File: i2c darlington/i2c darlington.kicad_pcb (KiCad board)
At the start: 2 copper layers, 131.2 x 55 mm, 48 parts, among them IC1 ULN2074B, IC2 ULN2074B, IC3 ULN2074B, IC4 ULN2074B, J1 to qwiic breakout, J2 high current ground, J3 Conn_01x04, J4 Conn_01x04, J5 Conn_01x04, J6 Conn_01x04, J7 Conn_01x01, J8 Conn_01x01, J9 Conn_01x01, U1 PCA9685PW

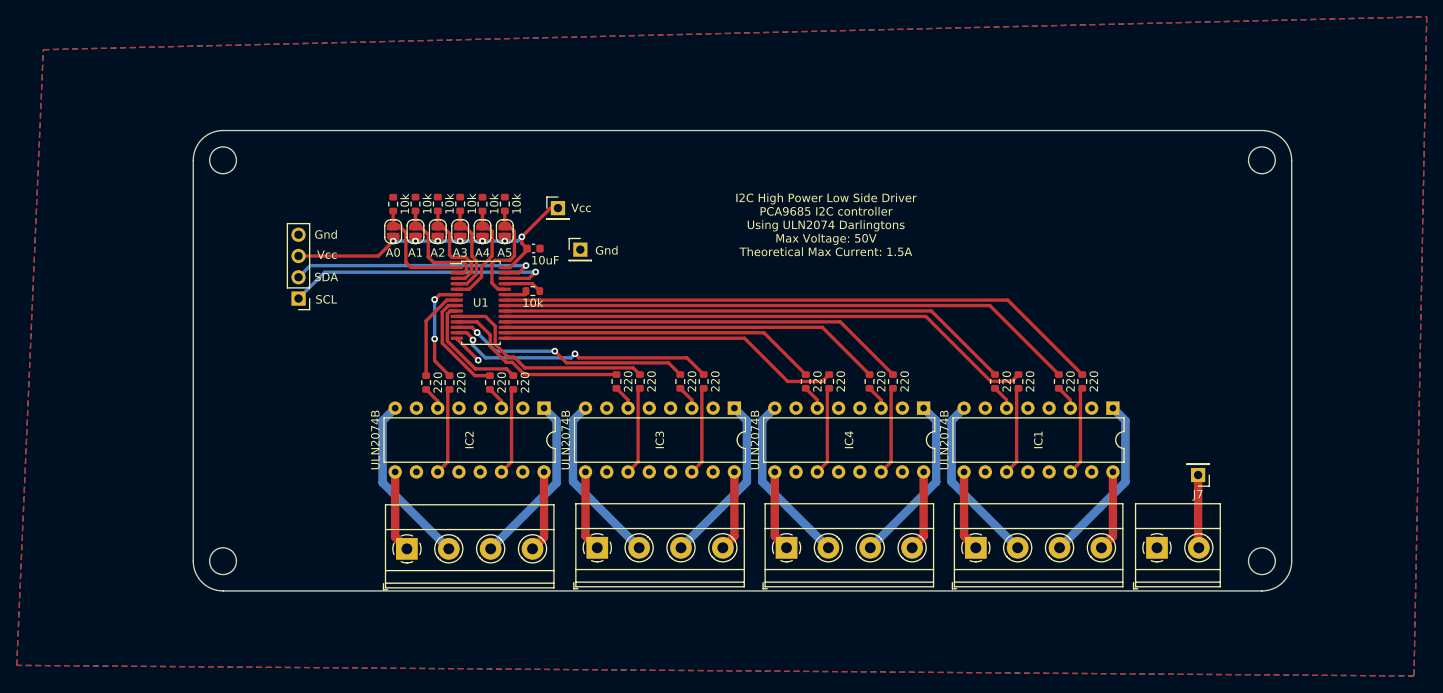
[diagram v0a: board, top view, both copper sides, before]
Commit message: shrank boards
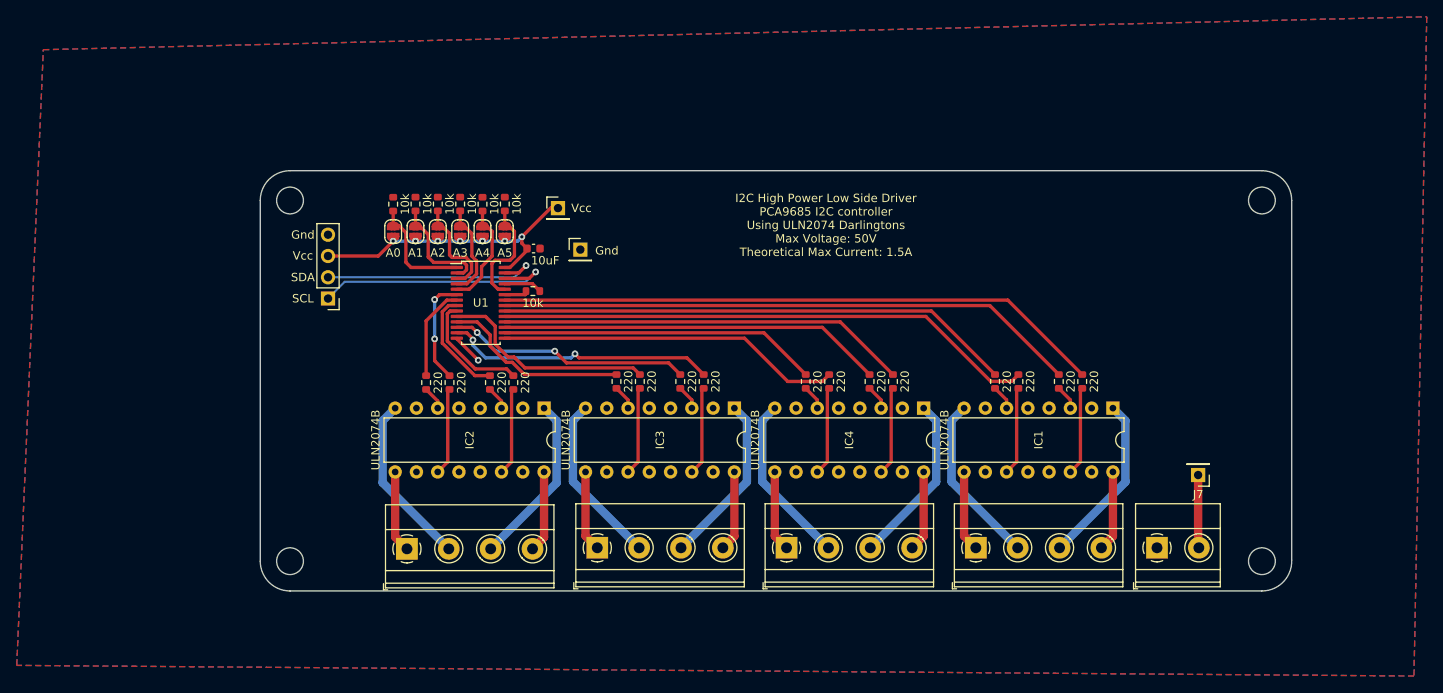
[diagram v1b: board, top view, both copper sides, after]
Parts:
- moved REF** 9.33 mm to (21.5, 123.3)
- moved REF** 8.00 mm to (21.5, 166.4)
- moved REF** 4.80 mm to (137.5, 123.3)
- moved J1 3.52 mm to (26.0, 135.0)
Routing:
- net /sda: track 30.7 -> 27.1 mm
- net VCC: track 38.7 -> 35.2 mm
- net /scl: track 33.6 -> 30.2 mm
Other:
- board size 131.2 x 55 mm -> 123.2 x 50.2 mm

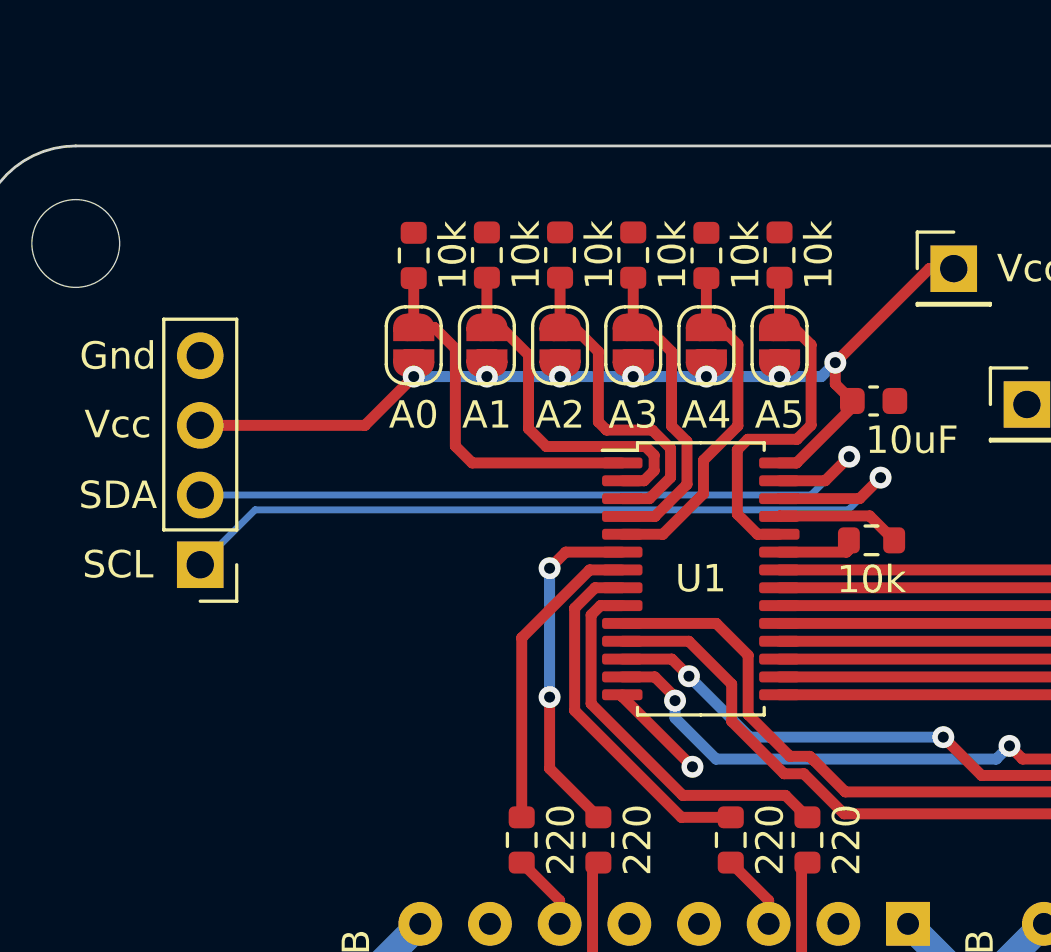
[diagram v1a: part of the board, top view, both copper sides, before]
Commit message: added qwiic connectors to boards as well as breakout connector
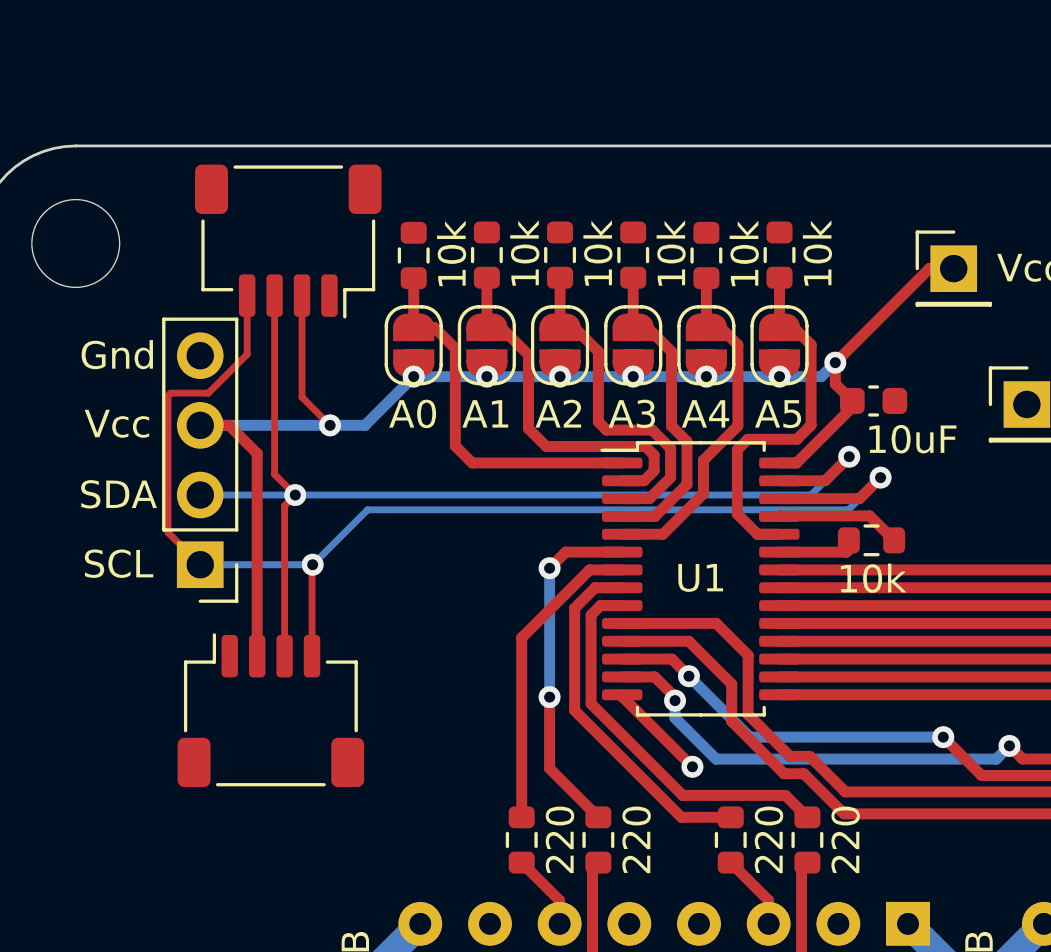
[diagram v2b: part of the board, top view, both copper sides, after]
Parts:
- added J10: qwiic 1, Connector_JST:JST_SH_SM04B-SRSS-TB_1x04-1MP_P1.00mm_Horizontal, F.Cu at (29.2, 123.2)
- added J11: qwiic 2, Connector_JST:JST_SH_SM04B-SRSS-TB_1x04-1MP_P1.00mm_Horizontal, F.Cu at (28.6, 140.3)
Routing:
- net /scl: track 30.2 -> 45.8 mm, vias 1 -> 2
- net VCC: track 35.2 -> 50.3 mm, vias 7 -> 8
- net /sda: track 27.1 -> 40.8 mm, vias 1 -> 2
